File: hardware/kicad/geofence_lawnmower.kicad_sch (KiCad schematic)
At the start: 20 parts, among them J1 Raspberry Pi 5 (J8 40-pin GPI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, U1 NEO-M8N GPS, U2 HC-SR04 (Front)

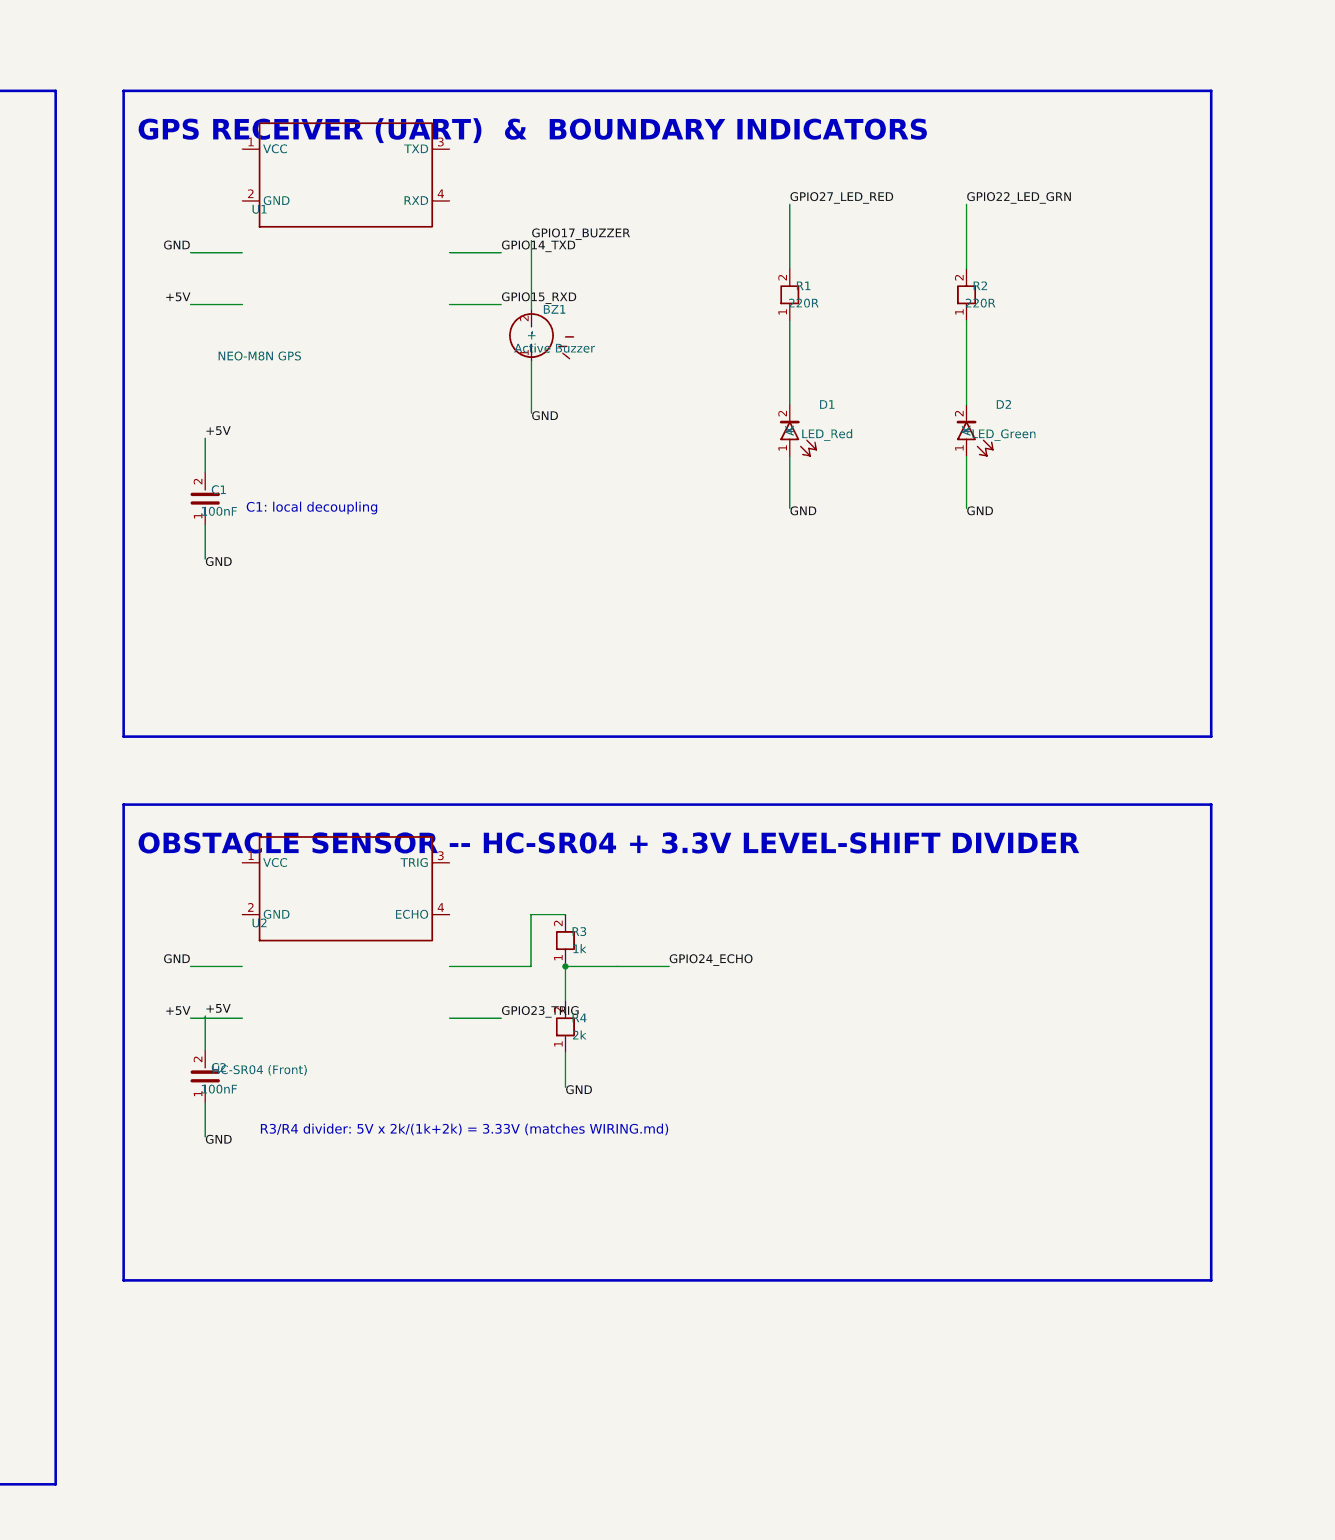
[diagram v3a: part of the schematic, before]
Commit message: fix: Clear remaining title overlap on the GPS and ultrasonic zones
Same issue as the Pi header (frame label too close to the module's top),
just smaller since these are 4-pin modules -- a 14mm gap wasn't quite
enough. Pushed the GPS module and HC-SR04 + divider down further, moved
their decoupling caps down to match, and grew both frames to fit.

Co-Authored-By: Claude Sonnet 5 <noreply@anthropic.com>
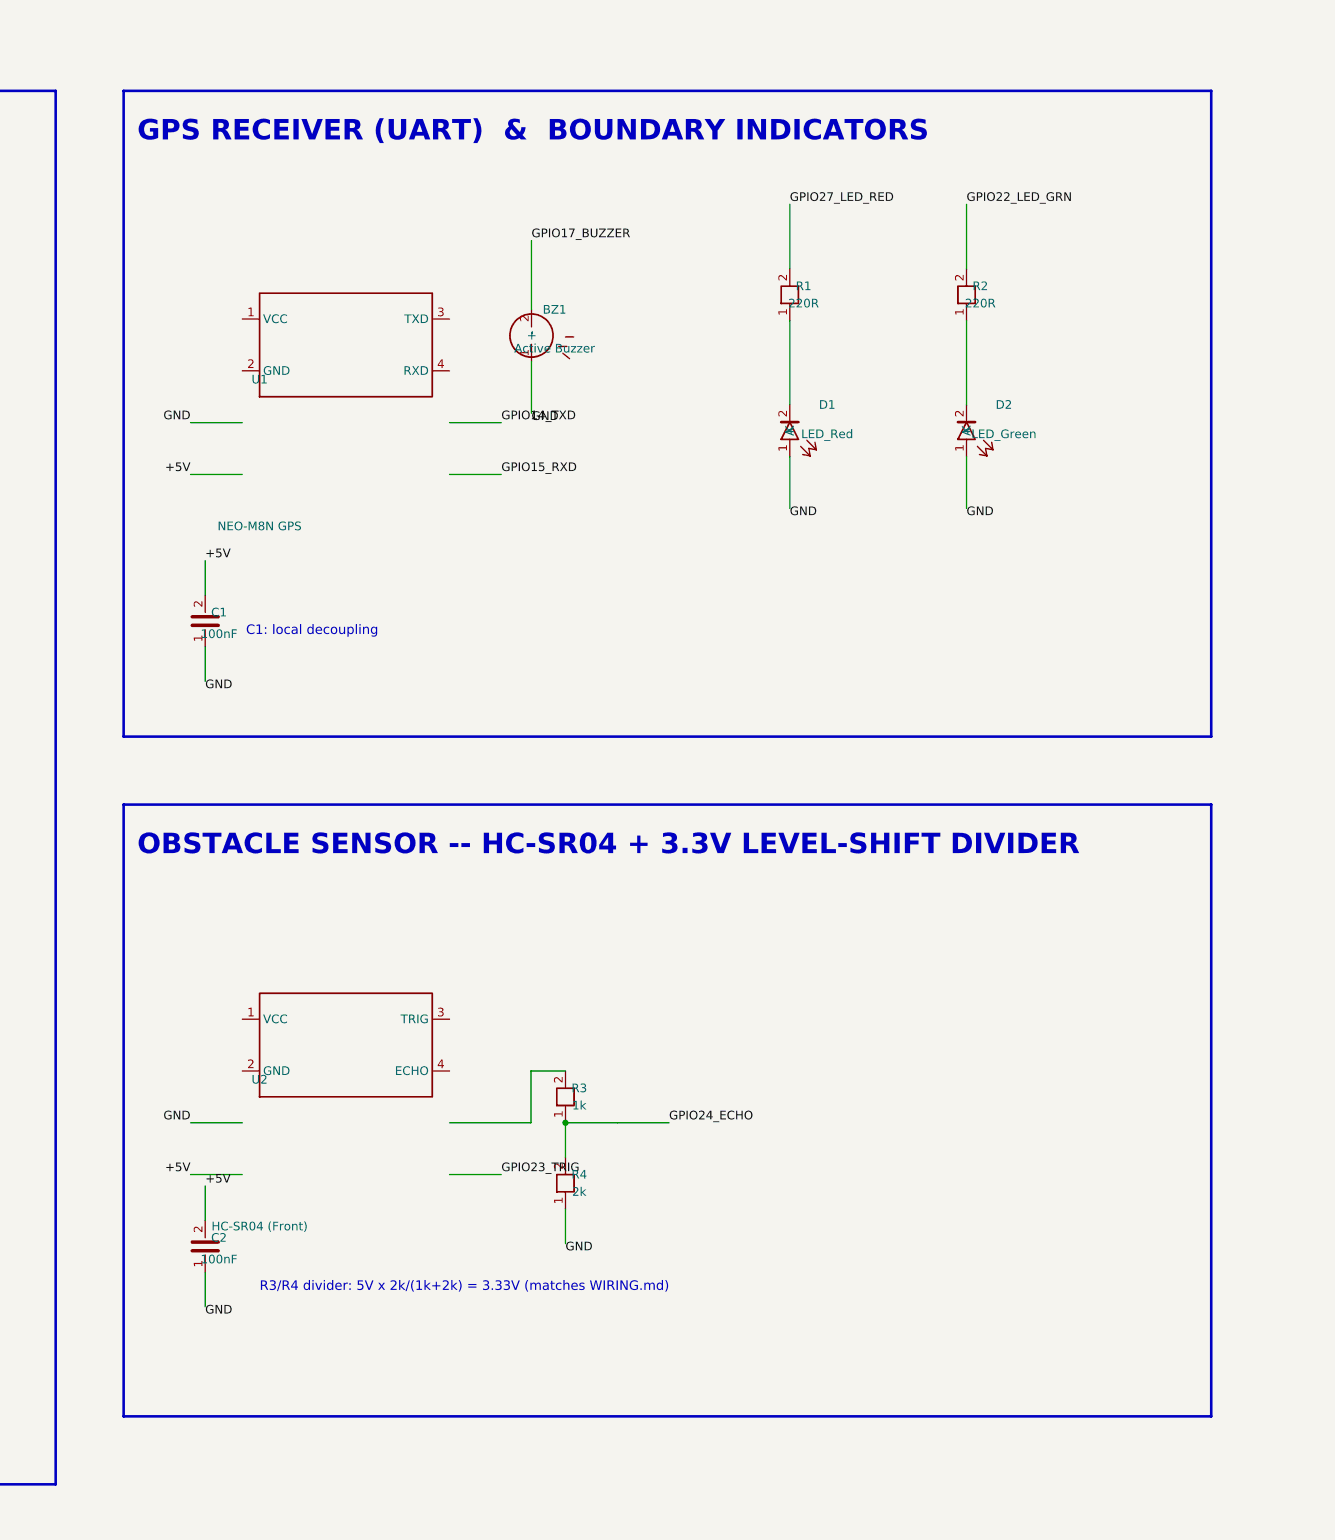
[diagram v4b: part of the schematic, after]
